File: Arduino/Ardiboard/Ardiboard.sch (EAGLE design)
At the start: 13 parts, among them IC1 ATMEGA168-20P, J1 1X5, Q2 AZ1086H-5.0, Q3 AZ1086H-3.3, U1 ARDUINOR3-BPLACE

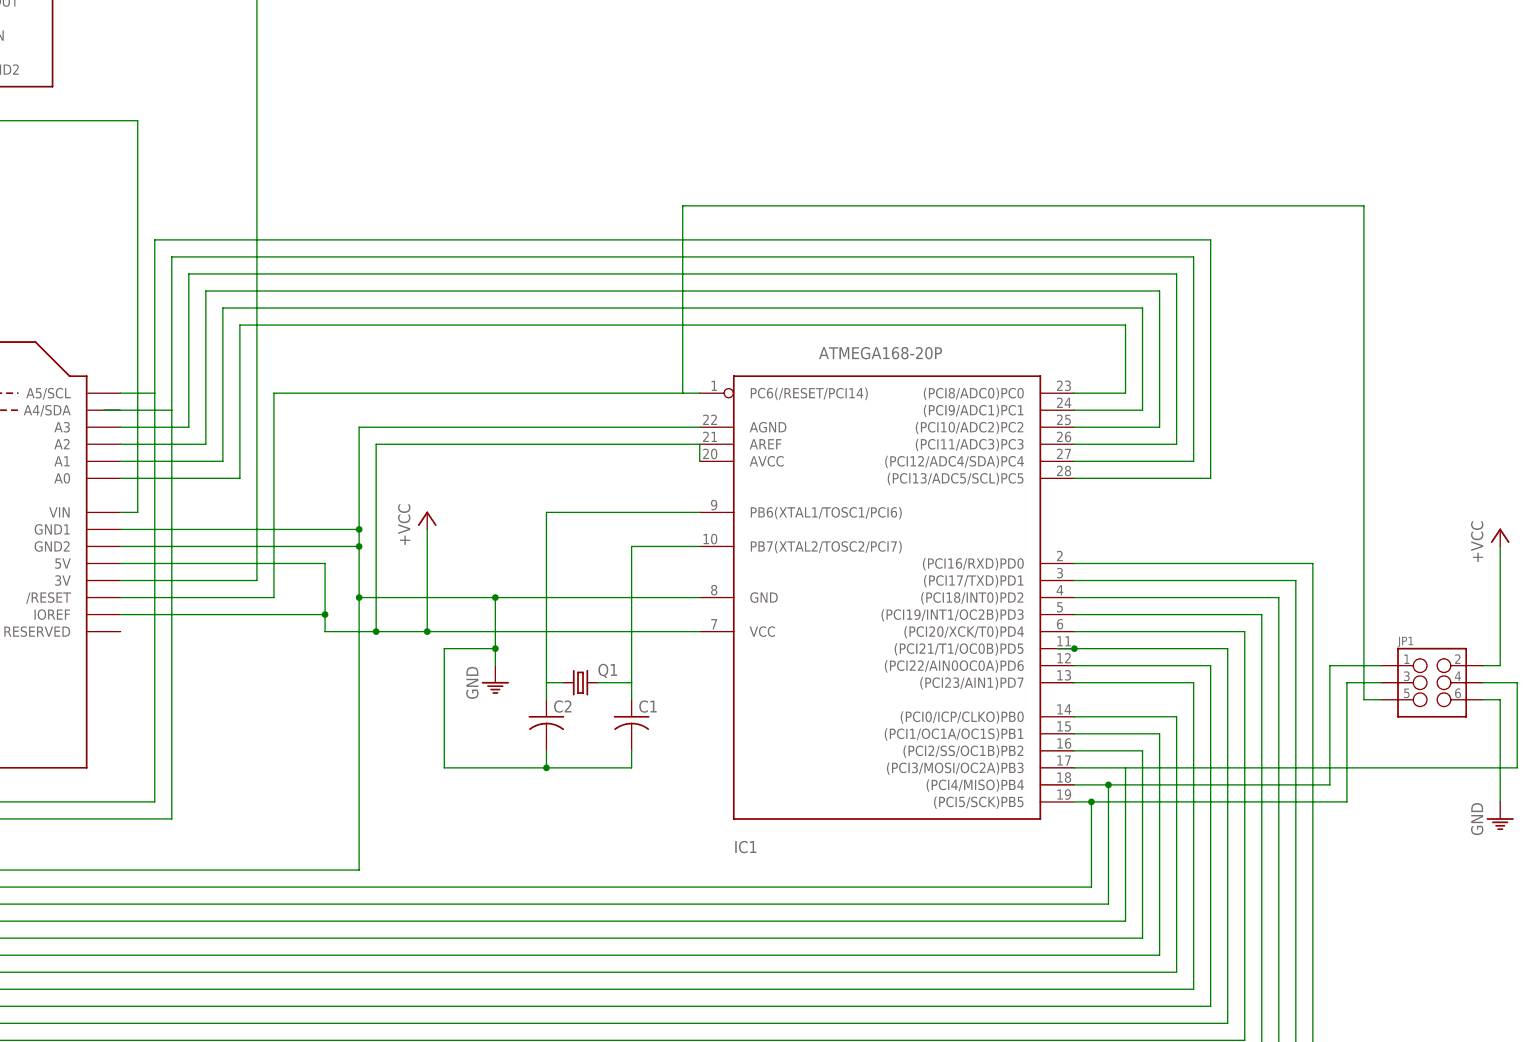
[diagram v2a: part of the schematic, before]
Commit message: added pull up resistor on reset, and 3.3V regulator pulls from output of 5V, not sure if I'll keep or change that.  Removed Ardiboard.brd file since new components were added.
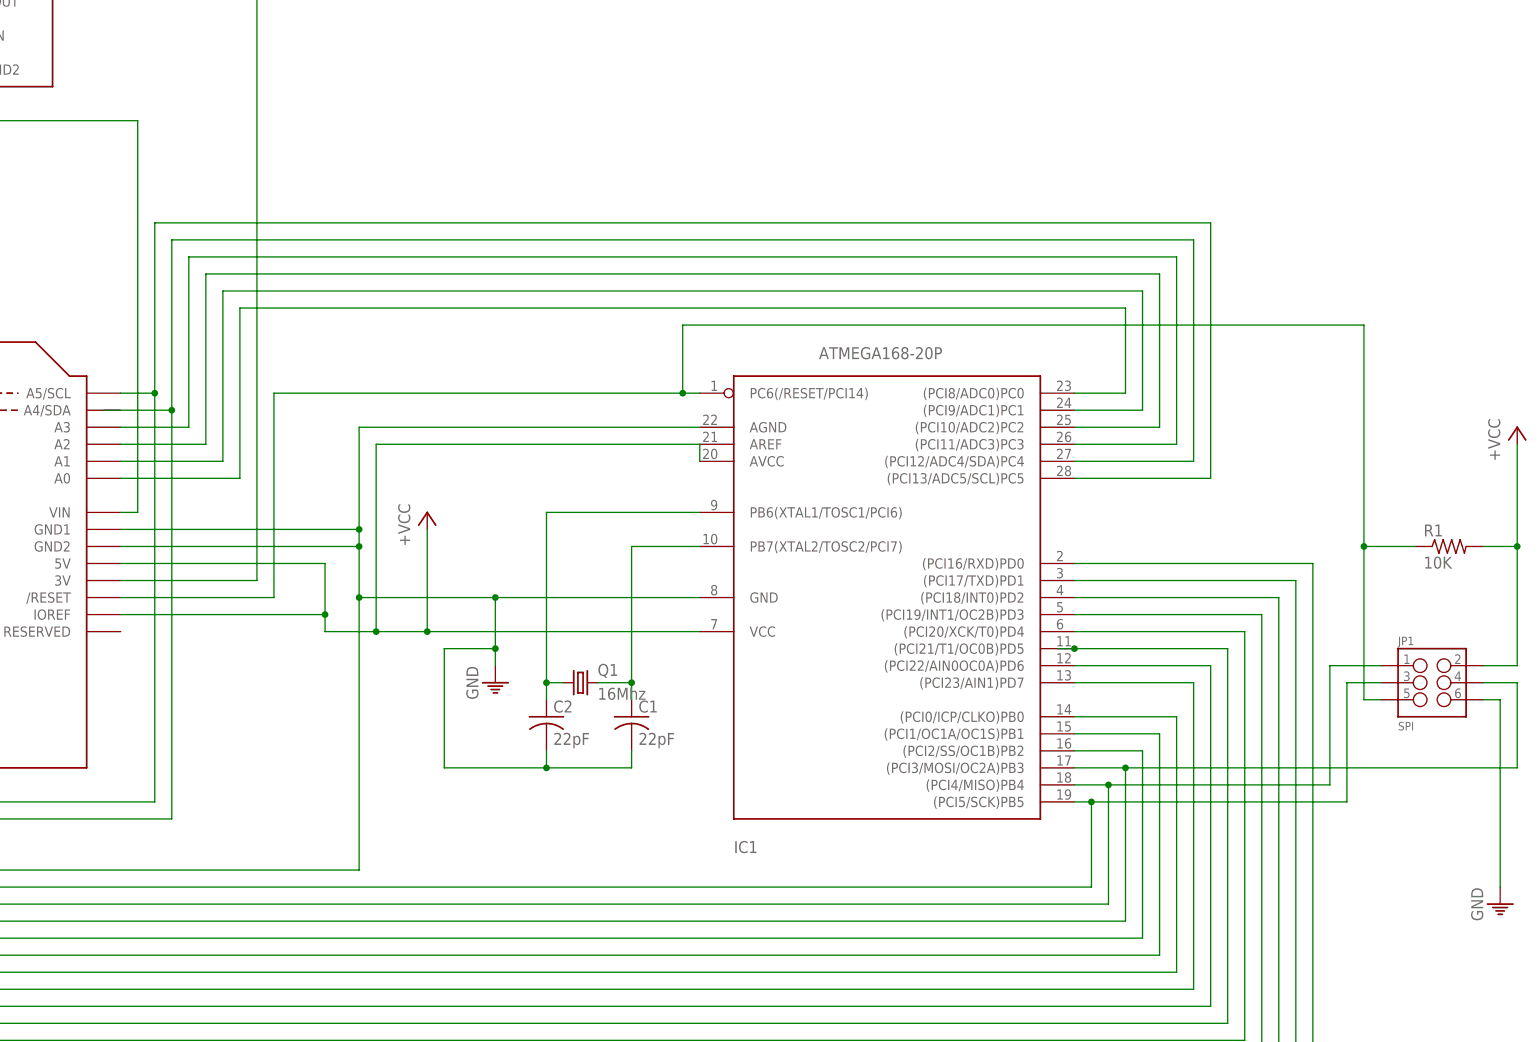
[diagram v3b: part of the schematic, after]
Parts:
- added R1: 10K, rcl:R-US_0207/10
- C1, C2: value (none) -> 22pF
- JP1: value (none) -> SPI
- Q1: value (none) -> 16Mhz
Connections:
- net +5V: now also R1.2
- net N$22: now also R1.1
